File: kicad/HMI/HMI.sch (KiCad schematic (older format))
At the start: 48 parts, among them J1 ENCODER, J2 SWD, J3 DEM 128128A TMH-PW-N, J4 RIBBON, SW1 SW_Push, SW10 SW_Push, SW11 SW_Push, SW12 SW_Push, SW13 SW_Push, SW14 SW_Push, SW15 SW_Push, SW16 SW_Push, SW17 SW_Push, SW18 SW_Push, SW19 SW_Push, SW2 SW_Push, SW20 SW_Push, SW3 SW_Push, SW4 SW_Push, SW5 SW_Push, SW6 SW_Push, SW7 SW_Push, SW8 SW_Push, SW9 SW_Push, U1 STM32L011K4Tx, X1 ASV-4.000MHZ-EJ-T

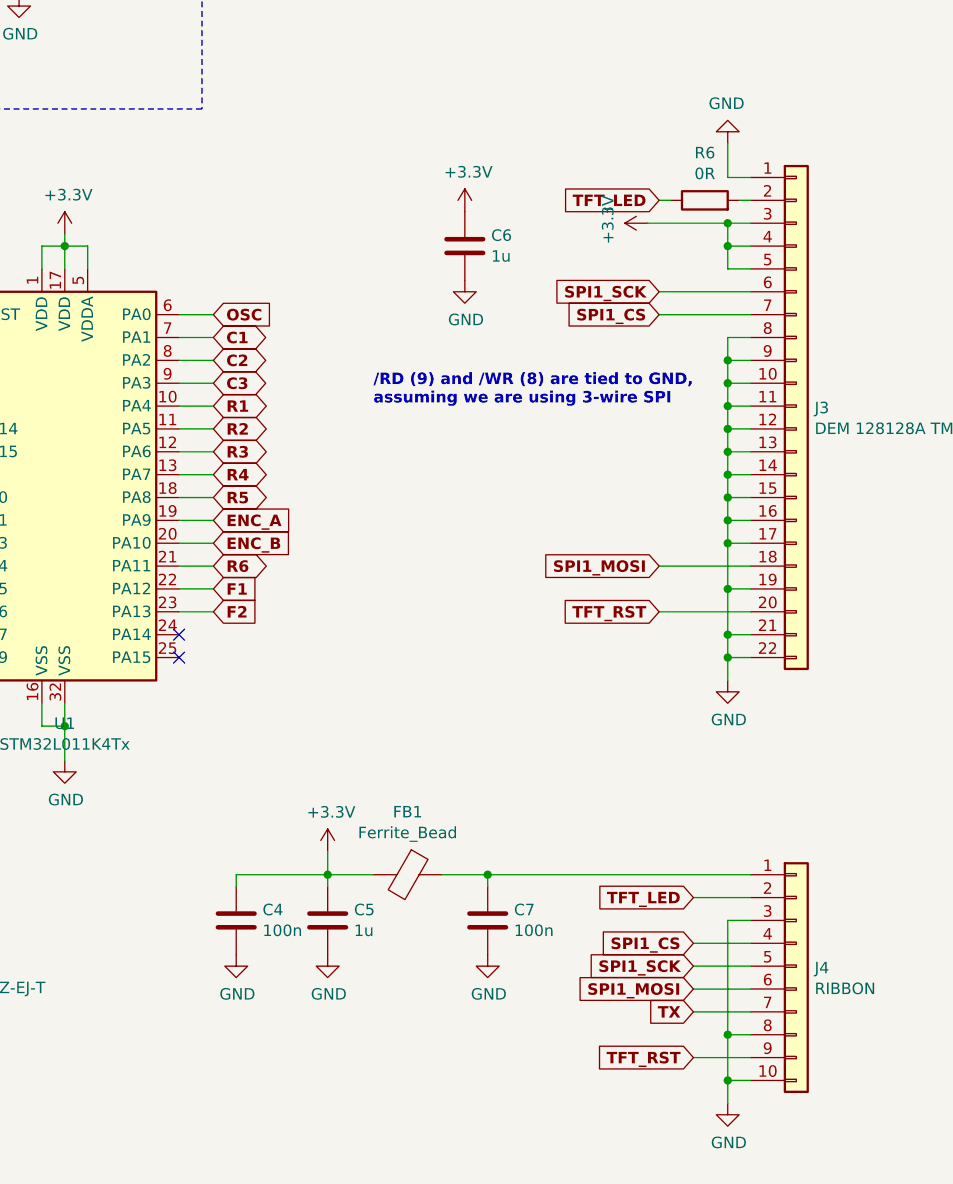
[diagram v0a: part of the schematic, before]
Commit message: added 5V line to the HMI ribbon
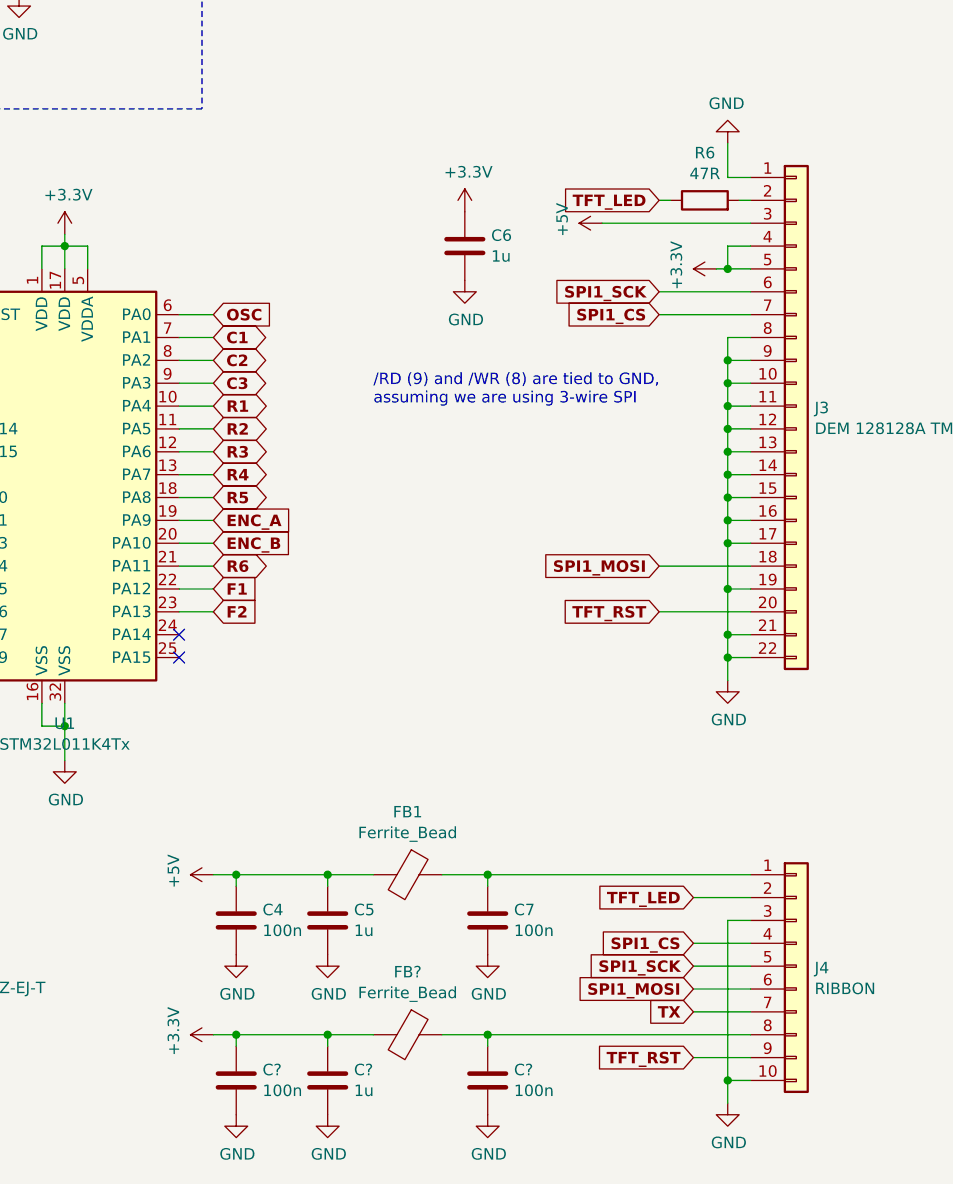
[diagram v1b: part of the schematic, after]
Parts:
- added C? (x2): 100n, Capacitor_SMD:C_0603_1608Metric, symbol Device:C
- added C?: 1u, Capacitor_SMD:C_0603_1608Metric, symbol Device:C
- added FB?: Ferrite_Bead, Inductor_SMD:L_0603_1608Metric, symbol Device:Ferrite_Bead
- R6: value 0R -> 47R
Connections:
- net +3V3: now also C?.1, C?.1, FB?.2; no longer C4.1, C5.1, FB1.2, J3.3 (Pin_3)
- net GND: now also C?.2, C?.2, C?.2; no longer J4.8 (Pin_8)
- new net: C?.1, FB?.1, J4.8 (Pin_8)
- new net +5V: C4.1, C5.1, FB1.2, J3.3 (Pin_3)
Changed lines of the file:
@@
 Wire Wire Line
 	3850 6250 3850 6300
-Wire Wire Line
-	3850 6250 3850 6150
 Connection ~ 3850 6250
 $Comp
 L power:+3.3V #PWR011
 U 1 1 5E38B8EA
-P 3850 6150
-F 0 "#PWR011" H 3850 6000 50  0001 C CNN
-F 1 "+3.3V" H 3865 6323 50  0000 C CNN
-F 2 "" H 3850 6150 50  0001 C CNN
-F 3 "" H 3850 6150 50  0001 C CNN
-	1    3850 6150
-	1    0    0    -1
-$EndComp
-Wire Wire Line
-	5700 6950 5600 6950
+P 3350 6950
+F 0 "#PWR011" H 3350 6800 50  0001 C CNN
+F 1 "+3.3V" H 3365 7123 50  0000 C CNN
+F 2 "" H 3350 6950 50  0001 C CNN
+F 3 "" H 3350 6950 50  0001 C CNN
+	1    3350 6950
+	0    -1   -1   0
+$EndComp
 Text GLabel 5450 6350 0    50   Input ~ 10
 TFT_LED
@@
 L power:+3.3V #PWR018
 U 1 1 5E4BBF2E
-P 5250 3400
-F 0 "#PWR018" H 5250 3250 50  0001 C CNN
-F 1 "+3.3V" H 5265 3573 50  0000 C CNN
-F 2 "" H 5250 3400 50  0001 C CNN
-F 3 "" H 5250 3400 50  0001 C CNN
-	1    5250 3400
+P 5550 3600
+F 0 "#PWR018" H 5550 3450 50  0001 C CNN
+F 1 "+3.3V" H 5565 3773 50  0000 C CNN
+F 2 "" H 5550 3600 50  0001 C CNN
+F 3 "" H 5550 3600 50  0001 C CNN
+	1    5550 3600
 	0    -1   -1   0
 $EndComp
@@
 P 5500 3300
 F 0 "R6" V 5707 3300 50  0000 C CNN
-F 1 "0R" V 5616 3300 50  0000 C CNN
+F 1 "47R" V 5616 3300 50  0000 C CNN
 F 2 "Resistor_SMD:R_0603_1608Metric" V 5430 3300 50  0001 C CNN
 F 3 "~" H 5500 3300 50  0001 C CNN
@@
 TFT_LED
 Wire Wire Line
-	5250 3400 5600 3400
-Wire Wire Line
 	5700 3500 5600 3500
 Wire Wire Line
-	5600 3500 5600 3400
-Connection ~ 5600 3400
-Wire Wire Line
-	5600 3400 5700 3400
-Wire Wire Line
 	5700 3600 5600 3600
 Wire Wire Line
 	5600 3600 5600 3500
-Connection ~ 5600 3500
 Wire Wire Line
 	5700 3700 5300 3700
@@
 Wire Wire Line
 	5600 3050 5600 3200
-Text Notes 4050 4200 0    50   ~ 10
+Text Notes 4050 4200 0    50   ~ 0
 /RD (9) and /WR (8) are tied to GND,\nassuming we are using 3-wire SPI
 Wire Wire Line
@@
 Wire Wire Line
 	5450 6850 5700 6850
-Wire Wire Line
-	5600 7150 5600 6950
 Connection ~ 5600 7150
 Wire Wire Line
-	5600 6950 5600 6450
-Connection ~ 5600 6950
-Wire Wire Line
 	5600 6450 5700 6450
+$Comp
+L power:+5V #PWR?
+U 1 1 5E4E30CF
+P 5050 3400
+F 0 "#PWR?" H 5050 3250 50  0001 C CNN
+F 1 "+5V" H 5065 3573 50  0000 C CNN
+F 2 "" H 5050 3400 50  0001 C CNN
+F 3 "" H 5050 3400 50  0001 C CNN
+	1    5050 3400
+	0    -1   -1   0
+$EndComp
+Wire Wire Line
+	5050 3400 5700 3400
+Wire Wire Line
+	5550 3600 5600 3600
+Connection ~ 5600 3600
+Wire Wire Line
+	5600 6450 5600 7150
+$Comp
+L power:+5V #PWR?
+U 1 1 5E56E379
+P 3350 6250
+F 0 "#PWR?" H 3350 6100 50  0001 C CNN
+F 1 "+5V" H 3365 6423 50  0000 C CNN
+F 2 "" H 3350 6250 50  0001 C CNN
+F 3 "" H 3350 6250 50  0001 C CNN
+	1    3350 6250
+	0    -1   -1   0
+$EndComp
+$Comp
+L Device:C C?
+U 1 1 5E583B34
+P 4550 7150
+F 0 "C?" H 4665 7196 50  0000 L CNN
+F 1 "100n" H 4665 7105 50  0000 L CNN
+F 2 "Capacitor_SMD:C_0603_1608Metric" H 4588 7000 50  0001 C CNN
+F 3 "~" H 4550 7150 50  0001 C CNN
+	1    4550 7150
+	1    0    0    -1
+$EndComp
+$Comp
+L Device:Ferrite_Bead FB?
+U 1 1 5E583B3A
+P 4200 6950
+F 0 "FB?" V 3926 6950 50  0000 C CNN
+F 1 "Ferrite_Bead" V 4017 6950 50  0000 C CNN
+F 2 "Inductor_SMD:L_0603_1608Metric" V 4130 6950 50  0001 C CNN
+F 3 "~" H 4200 6950 50  0001 C CNN
+	1    4200 6950
+	0    1    1    0
+$EndComp
+$Comp
+L Device:C C?
+U 1 1 5E583B40
+P 3850 7150
+F 0 "C?" H 3965 7196 50  0000 L CNN
+F 1 "1u" H 3965 7105 50  0000 L CNN
+F 2 "Capacitor_SMD:C_0603_1608Metric" H 3888 7000 50  0001 C CNN
+F 3 "~" H 3850 7150 50  0001 C CNN
+	1    3850 7150
+	1    0    0    -1
+$EndComp
+$Comp
+L Device:C C?
+U 1 1 5E583B46
+P 3450 7150
+F 0 "C?" H 3565 7196 50  0000 L CNN
+F 1 "100n" H 3565 7105 50  0000 L CNN
+F 2 "Capacitor_SMD:C_0603_1608Metric" H 3488 7000 50  0001 C CNN
+F 3 "~" H 3450 7150 50  0001 C CNN
+	1    3450 7150
+	1    0    0    -1
+$EndComp
+$Comp
+L power:GND #PWR?
+U 1 1 5E583B4C
+P 3850 7300
+F 0 "#PWR?" H 3850 7050 50  0001 C CNN
+F 1 "GND" H 3855 7127 50  0000 C CNN
+F 2 "" H 3850 7300 50  0001 C CNN
+F 3 "" H 3850 7300 50  0001 C CNN
+	1    3850 7300
+	1    0    0    -1
+$EndComp
+Wire Wire Line
+	3850 6950 3850 7000
+Connection ~ 3850 6950
+Wire Wire Line
+	3850 6950 4050 6950
+$Comp
+L power:GND #PWR?
+U 1 1 5E583B56
+P 4550 7300
+F 0 "#PWR?" H 4550 7050 50  0001 C CNN
+F 1 "GND" H 4555 7127 50  0000 C CNN
+F 2 "" H 4550 7300 50  0001 C CNN
+F 3 "" H 4550 7300 50  0001 C CNN
+	1    4550 7300
+	1    0    0    -1
+$EndComp
+Wire Wire Line
+	4350 6950 4550 6950
+Wire Wire Line
+	4550 7000 4550 6950
+Connection ~ 4550 6950
+$Comp
+L power:GND #PWR?
+U 1 1 5E583B5F
+P 3450 7300
+F 0 "#PWR?" H 3450 7050 50  0001 C CNN
+F 1 "GND" H 3455 7127 50  0000 C CNN
+F 2 "" H 3450 7300 50  0001 C CNN
+F 3 "" H 3450 7300 50  0001 C CNN
+	1    3450 7300
+	1    0    0    -1
+$EndComp
+Wire Wire Line
+	3450 7000 3450 6950
+Wire Wire Line
+	3450 6950 3850 6950
+Wire Wire Line
+	4550 6950 5700 6950
+Wire Wire Line
+	3450 6250 3350 6250
+Connection ~ 3450 6250
+Wire Wire Line
+	3450 6950 3350 6950
+Connection ~ 3450 6950
 $EndSCHEMATC

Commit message: cleanup, annotation
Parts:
- removed C2, C3: 10n, Capacitor_SMD:C_0603_1608Metric, symbol Device:C
- removed J1: ENCODER, Connector_PinSocket_2.54mm:PinSocket_1x03_P2.54mm_Vertical, symbol Connector_Generic:Conn_01x03
- removed R1, R2, R3, R4: 10k, Resistor_SMD:R_0603_1608Metric, symbol Device:R
- J2: footprint Connector_PinSocket_2.54mm:PinSocket_1x04_P2.54mm_Vertical -> Connector_PinHeader_1.27mm:PinHeader_1x04_P1.27mm_Vertical
- SW1, SW10, SW11, SW12, SW13, SW14, SW15, SW16, SW17, SW18, SW19, SW2, SW20, SW3, SW4, SW5, SW6, SW7, SW8, SW9: footprint (none) -> Button_Switch_SMD:SW_Push_1P1T_NO_CK_KMR2
- gave numbers to parts that had none: 4
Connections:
- net ENC_A: no longer names the net of U1.19 (PA9)
- net ENC_B: no longer names the net of U1.20 (PA10)
- no-connect marks 11 -> 13
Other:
- note removed: "We are using a pot instead - so no longer needed"
- moved on the sheet: U1

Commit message: corrected FPC footprint assignment
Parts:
- J3: footprint (none) -> Connector_FFC-FPC:Hirose_FH12-22S-0.5SH_1x22-1MP_P0.50mm_Horizontal
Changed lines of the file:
@@
 F 0 "J3" H 5980 4192 50  0000 L CNN
 F 1 "DEM 128128A TMH-PW-N" H 5980 4101 50  0000 L CNN
-F 2 "" H 5900 4200 50  0001 C CNN
+F 2 "Connector_FFC-FPC:Hirose_FH12-22S-0.5SH_1x22-1MP_P0.50mm_Horizontal" H 5900 4200 50  0001 C CNN
 F 3 "~" H 5900 4200 50  0001 C CNN
 	1    5900 4200

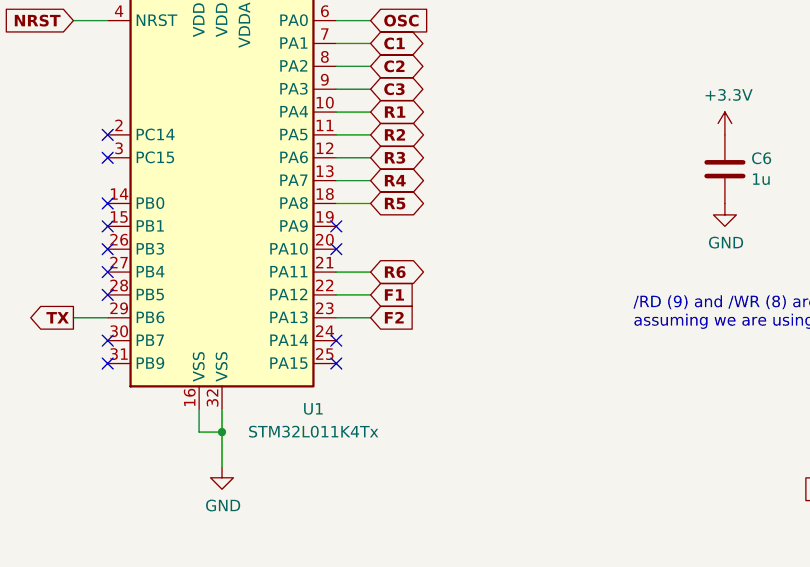
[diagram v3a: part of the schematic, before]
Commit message: added SWD pins to the micro, started laying out the board
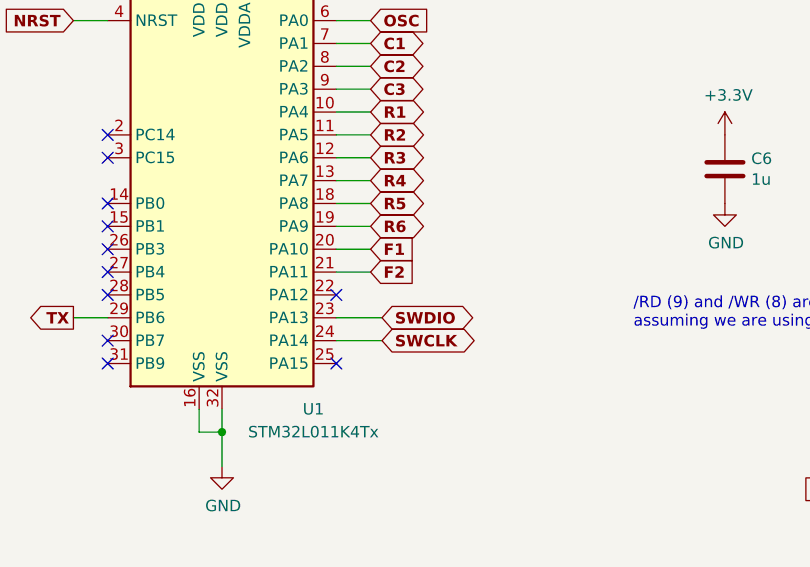
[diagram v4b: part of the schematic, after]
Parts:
- J4: footprint (none) -> Connector_FFC-FPC:Hirose_FH12-10S-0.5SH_1x10-1MP_P0.50mm_Horizontal
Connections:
- net F1: now also U1.20 (PA10); no longer U1.22 (PA12)
- net F2: now also U1.21 (PA11); no longer U1.23 (PA13)
- net R6: now also U1.19 (PA9); no longer U1.21 (PA11)
- net SWCLK: now also U1.24 (PA14)
- net SWDIO: now also U1.23 (PA13)
- no-connect marks 13 -> 11
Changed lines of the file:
@@
 	2750 3650 2900 3650
 Wire Wire Line
-	2750 3950 2900 3950
+	2750 3750 2900 3750
 Text GLabel 2900 3650 2    50   BiDi ~ 10
 R5
-Text GLabel 2900 3950 2    50   BiDi ~ 10
+Text GLabel 2900 3750 2    50   BiDi ~ 10
 R6
-NoConn ~ 2750 4250
-NoConn ~ 2750 4350
 NoConn ~ 1750 4250
 NoConn ~ 1750 4350
@@
 F 0 "J4" H 5980 6642 50  0000 L CNN
 F 1 "RIBBON" H 5980 6551 50  0000 L CNN
-F 2 "" H 5900 6650 50  0001 C CNN
+F 2 "Connector_FFC-FPC:Hirose_FH12-10S-0.5SH_1x10-1MP_P0.50mm_Horizontal" H 5900 6650 50  0001 C CNN
 F 3 "~" H 5900 6650 50  0001 C CNN
 	1    5900 6650
@@
 	6500 1550 6350 1550
 Wire Wire Line
-	2900 4050 2750 4050
-Wire Wire Line
-	2900 4150 2750 4150
-Text GLabel 2900 4050 2    50   Input ~ 10
+	2900 3850 2750 3850
+Wire Wire Line
+	2900 3950 2750 3950
+Text GLabel 2900 3850 2    50   Input ~ 10
 F1
-Text GLabel 2900 4150 2    50   Input ~ 10
+Text GLabel 2900 3950 2    50   Input ~ 10
 F2
 Text GLabel 6850 2050 3    50   Input ~ 10
@@
 	3450 6950 3350 6950
 Connection ~ 3450 6950
-NoConn ~ 2750 3750
-NoConn ~ 2750 3850
+Wire Wire Line
+	2750 4150 2950 4150
+Wire Wire Line
+	2750 4250 2950 4250
+Text GLabel 2950 4150 2    50   BiDi ~ 10
+SWDIO
+Text GLabel 2950 4250 2    50   BiDi ~ 10
+SWCLK
+NoConn ~ 2750 4050
+NoConn ~ 2750 4350
 $EndSCHEMATC

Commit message: HMI - changed SW1 and SW14 button footprint; Mainboard - further changes; TR-9 library, correcting footprint
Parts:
- SW1, SW14: footprint Button_Switch_SMD:SW_Push_1P1T_NO_CK_KMR2 -> Button_Switch_THT:SW_Tactile_SKHH_Angled
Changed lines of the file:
@@
 F 0 "SW1" V 8604 1348 50  0000 L CNN
 F 1 "SW_Push" V 8695 1348 50  0000 L CNN
-F 2 "Button_Switch_SMD:SW_Push_1P1T_NO_CK_KMR2" H 8650 1400 50  0001 C CNN
+F 2 "Button_Switch_THT:SW_Tactile_SKHH_Angled" H 8650 1400 50  0001 C CNN
 F 3 "~" H 8650 1400 50  0001 C CNN
 	1    8650 1200
@@
 F 0 "SW14" V 9654 1348 50  0000 L CNN
 F 1 "SW_Push" V 9745 1348 50  0000 L CNN
-F 2 "Button_Switch_SMD:SW_Push_1P1T_NO_CK_KMR2" H 9700 1400 50  0001 C CNN
+F 2 "Button_Switch_THT:SW_Tactile_SKHH_Angled" H 9700 1400 50  0001 C CNN
 F 3 "~" H 9700 1400 50  0001 C CNN
 	1    9700 1200

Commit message: HMI: added design of PCB -> plotted PDF -> plotted production output - Gerbers -> HMI is READY!!
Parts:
- added C9: 1u, Capacitor_SMD:C_0603_1608Metric, symbol Device:C
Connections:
- net +3V3: now also J3.18 (Pin_18), J3.19 (Pin_19), C9.1; no longer J3.4 (Pin_4), J3.5 (Pin_5)
- net +5V: now also J3.20 (Pin_20); no longer J3.3 (Pin_3)
- net GND: now also J3.2 (Pin_2), J3.4 (Pin_4), J3.6 (Pin_6), J3.7 (Pin_7), C9.2; no longer J3.16 (Pin_16), J3.17 (Pin_17), J3.19 (Pin_19), J3.21 (Pin_21)
- net SPI1_CS: now also J3.16 (Pin_16); no longer J3.7 (Pin_7)
- net SPI1_MOSI: now also J3.5 (Pin_5); no longer J3.18 (Pin_18)
- net SPI1_SCK: now also J3.17 (Pin_17); no longer J3.6 (Pin_6)
- net TFT_RST: now also J3.3 (Pin_3); no longer J3.20 (Pin_20)
- net at R6.2: now also J3.21 (Pin_21); no longer J3.2 (Pin_2)
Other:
- moved on the sheet: C6
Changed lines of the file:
@@
 L Connector_Generic:Conn_01x22 J3
 U 1 1 5E2A885D
-P 5900 4200
-F 0 "J3" H 5980 4192 50  0000 L CNN
-F 1 "DEM 128128A TMH-PW-N" H 5980 4101 50  0000 L CNN
-F 2 "Connector_FFC-FPC:Hirose_FH12-22S-0.5SH_1x22-1MP_P0.50mm_Horizontal" H 5900 4200 50  0001 C CNN
-F 3 "~" H 5900 4200 50  0001 C CNN
-	1    5900 4200
-	1    0    0    -1
+P 5900 4300
+F 0 "J3" H 5980 4292 50  0000 L CNN
+F 1 "DEM 128128A TMH-PW-N" H 5980 4201 50  0000 L CNN
+F 2 "Connector_FFC-FPC:Hirose_FH12-22S-0.5SH_1x22-1MP_P0.50mm_Horizontal" H 5900 4300 50  0001 C CNN
+F 3 "~" H 5900 4300 50  0001 C CNN
+	1    5900 4300
+	1    0    0    1
 $EndComp
 Text GLabel 8500 6050 3    50   BiDi ~ 10
@@
 L power:GND #PWR016
 U 1 1 5E23A966
-P 4450 3650
-F 0 "#PWR016" H 4450 3400 50  0001 C CNN
-F 1 "GND" H 4455 3477 50  0000 C CNN
-F 2 "" H 4450 3650 50  0001 C CNN
-F 3 "" H 4450 3650 50  0001 C CNN
-	1    4450 3650
+P 4200 3750
+F 0 "#PWR016" H 4200 3500 50  0001 C CNN
+F 1 "GND" H 4205 3577 50  0000 C CNN
+F 2 "" H 4200 3750 50  0001 C CNN
+F 3 "" H 4200 3750 50  0001 C CNN
+	1    4200 3750
 	1    0    0    -1
 $EndComp
@@
 L Device:C C6
 U 1 1 5E23AEBE
-P 4450 3500
-F 0 "C6" H 4565 3546 50  0000 L CNN
-F 1 "1u" H 4565 3455 50  0000 L CNN
-F 2 "Capacitor_SMD:C_0603_1608Metric" H 4488 3350 50  0001 C CNN
-F 3 "~" H 4450 3500 50  0001 C CNN
-	1    4450 3500
+P 4300 3500
+F 0 "C6" H 4415 3546 50  0000 L CNN
+F 1 "1u" H 4415 3455 50  0000 L CNN
+F 2 "Capacitor_SMD:C_0603_1608Metric" H 4338 3350 50  0001 C CNN
+F 3 "~" H 4300 3500 50  0001 C CNN
+	1    4300 3500
 	1    0    0    -1
 $EndComp
@@
 L power:+3.3V #PWR015
 U 1 1 5E23B479
-P 4450 3350
-F 0 "#PWR015" H 4450 3200 50  0001 C CNN
-F 1 "+3.3V" H 4465 3523 50  0000 C CNN
-F 2 "" H 4450 3350 50  0001 C CNN
-F 3 "" H 4450 3350 50  0001 C CNN
-	1    4450 3350
+P 4200 3250
+F 0 "#PWR015" H 4200 3100 50  0001 C CNN
+F 1 "+3.3V" H 4215 3423 50  0000 C CNN
+F 2 "" H 4200 3250 50  0001 C CNN
+F 3 "" H 4200 3250 50  0001 C CNN
+	1    4200 3250
 	1    0    0    -1
 $EndComp
@@
 U 1 1 5E2A8493
 P 5900 1800
-F 0 "R7" H 5970 1846 50  0000 L CNN
-F 1 "47k" H 5970 1755 50  0000 L CNN
+F 0 "R7" V 5900 1050 50  0000 L CNN
+F 1 "47k" V 5900 1200 50  0000 L CNN
 F 2 "Resistor_SMD:R_0603_1608Metric" V 5830 1800 50  0001 C CNN
 F 3 "~" H 5900 1800 50  0001 C CNN
@@
 U 1 1 5E2C0402
 P 6050 1800
-F 0 "R8" H 6120 1846 50  0000 L CNN
-F 1 "47k" H 6120 1755 50  0000 L CNN
+F 0 "R8" V 6050 1050 50  0000 L CNN
+F 1 "47k" V 6050 1200 50  0000 L CNN
 F 2 "Resistor_SMD:R_0603_1608Metric" V 5980 1800 50  0001 C CNN
 F 3 "~" H 6050 1800 50  0001 C CNN
@@
 U 1 1 5E2C057A
 P 6200 1800
-F 0 "R9" H 6270 1846 50  0000 L CNN
-F 1 "47k" H 6270 1755 50  0000 L CNN
+F 0 "R9" V 6200 1050 50  0000 L CNN
+F 1 "47k" V 6200 1200 50  0000 L CNN
 F 2 "Resistor_SMD:R_0603_1608Metric" V 6130 1800 50  0001 C CNN
 F 3 "~" H 6200 1800 50  0001 C CNN
@@
 U 1 1 5E2C0631
 P 6350 1800
-F 0 "R10" H 6420 1846 50  0000 L CNN
-F 1 "47k" H 6420 1755 50  0000 L CNN
+F 0 "R10" V 6350 1000 50  0000 L CNN
+F 1 "47k" V 6350 1200 50  0000 L CNN
 F 2 "Resistor_SMD:R_0603_1608Metric" V 6280 1800 50  0001 C CNN
 F 3 "~" H 6350 1800 50  0001 C CNN
@@
 U 1 1 5E2C075F
 P 6500 1800
-F 0 "R11" H 6570 1846 50  0000 L CNN
-F 1 "47k" H 6570 1755 50  0000 L CNN
+F 0 "R11" V 6500 1000 50  0000 L CNN
+F 1 "47k" V 6500 1200 50  0000 L CNN
 F 2 "Resistor_SMD:R_0603_1608Metric" V 6430 1800 50  0001 C CNN
 F 3 "~" H 6500 1800 50  0001 C CNN
@@
 U 1 1 5E2C0888
 P 6650 1800
-F 0 "R12" H 6720 1846 50  0000 L CNN
-F 1 "47k" H 6720 1755 50  0000 L CNN
+F 0 "R12" V 6650 1000 50  0000 L CNN
+F 1 "47k" V 6650 1200 50  0000 L CNN
 F 2 "Resistor_SMD:R_0603_1608Metric" V 6580 1800 50  0001 C CNN
 F 3 "~" H 6650 1800 50  0001 C CNN
@@
 U 1 1 5E2D9171
 P 6850 1800
-F 0 "R13" H 6920 1846 50  0000 L CNN
-F 1 "47k" H 6920 1755 50  0000 L CNN
+F 0 "R13" V 6850 1000 50  0000 L CNN
+F 1 "47k" V 6850 1200 50  0000 L CNN
 F 2 "Resistor_SMD:R_0603_1608Metric" V 6780 1800 50  0001 C CNN
 F 3 "~" H 6850 1800 50  0001 C CNN
@@
 U 1 1 5E2D92B9
 P 7000 1800
-F 0 "R14" H 7070 1846 50  0000 L CNN
-F 1 "47k" H 7070 1755 50  0000 L CNN
+F 0 "R14" V 7000 1000 50  0000 L CNN
+F 1 "47k" V 7000 1200 50  0000 L CNN
 F 2 "Resistor_SMD:R_0603_1608Metric" V 6930 1800 50  0001 C CNN
 F 3 "~" H 7000 1800 50  0001 C CNN
@@
 NoConn ~ 2750 4050
 NoConn ~ 2750 4350
+$Comp
+L Device:C C9
+U 1 1 5F2AFB96
+P 4050 3500
+F 0 "C9" H 3850 3550 50  0000 L CNN
+F 1 "1u" H 3850 3450 50  0000 L CNN
+F 2 "Capacitor_SMD:C_0603_1608Metric" H 4088 3350 50  0001 C CNN
+F 3 "~" H 4050 3500 50  0001 C CNN
+	1    4050 3500
+	1    0    0    -1
+$EndComp
+Wire Wire Line
+	4300 3350 4300 3250
+Wire Wire Line
+	4300 3250 4200 3250
+Wire Wire Line
+	4200 3250 4050 3250
+Wire Wire Line
+	4050 3250 4050 3350
+Connection ~ 4200 3250
+Wire Wire Line
+	4050 3650 4050 3750
+Wire Wire Line
+	4050 3750 4200 3750
+Wire Wire Line
+	4200 3750 4300 3750
+Wire Wire Line
+	4300 3750 4300 3650
+Connection ~ 4200 3750
 $EndSCHEMATC
